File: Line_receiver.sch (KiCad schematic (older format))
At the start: 15 parts, among them U15 LM4562

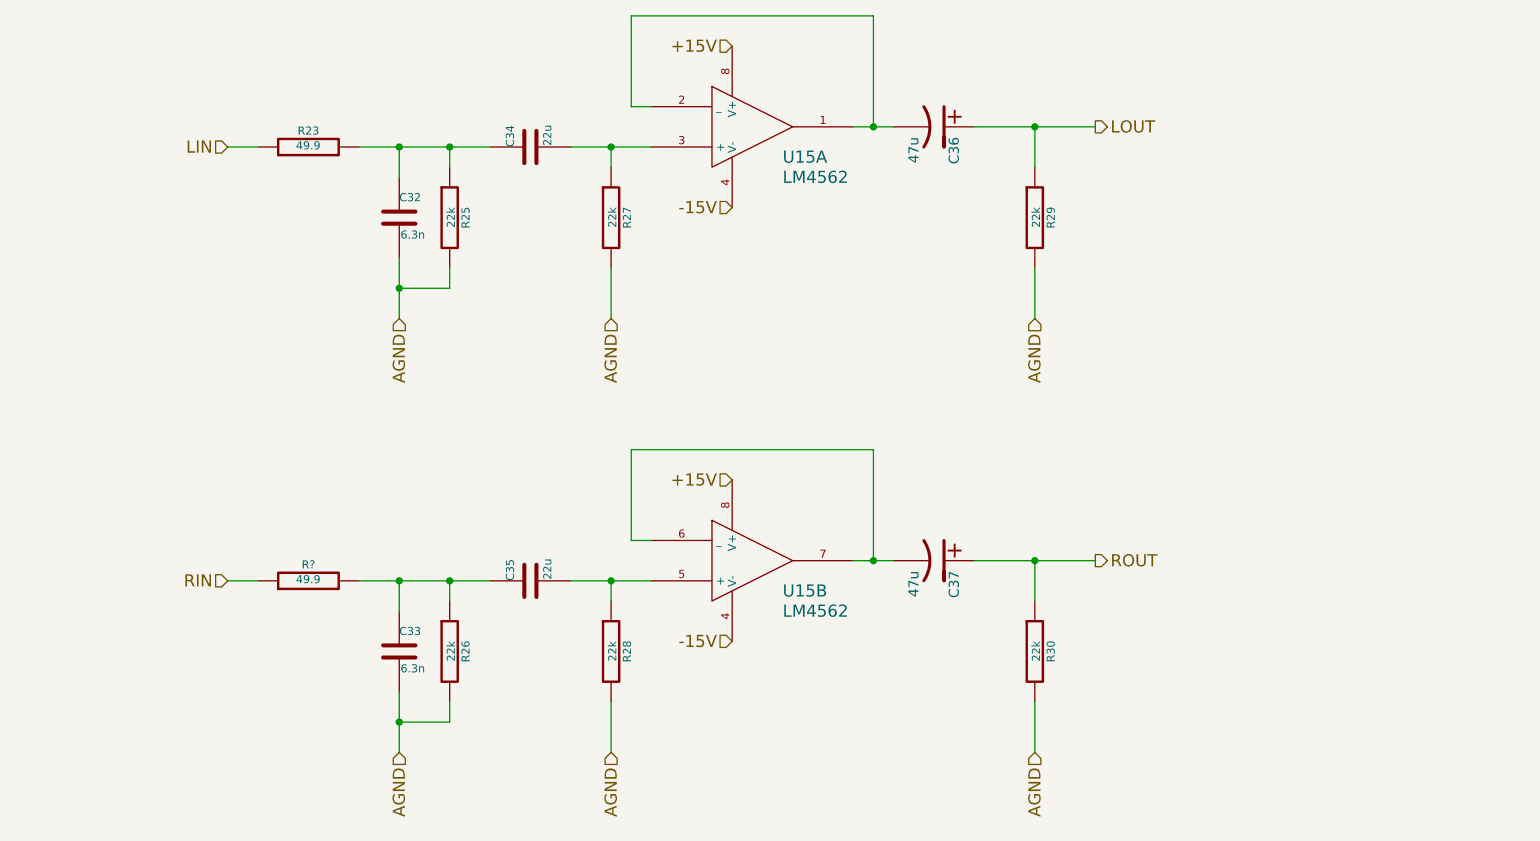
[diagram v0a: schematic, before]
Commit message: Further component specifications for the BOM.
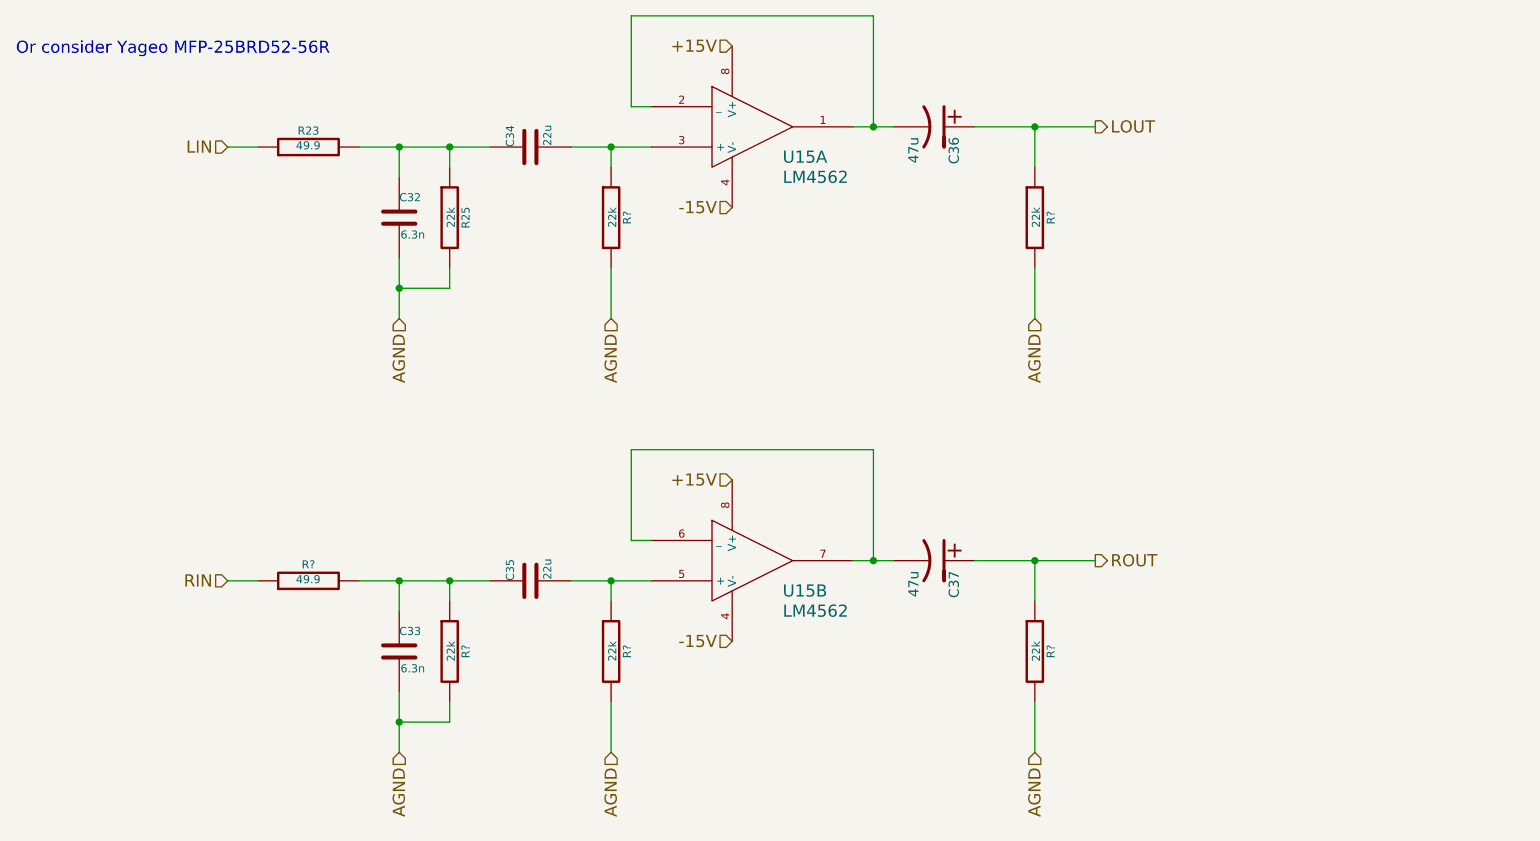
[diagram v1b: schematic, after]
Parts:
- removed R26, R27, R28, R29, R30: 22k, ~, symbol R
- added R? (x5): 22k, ~, symbol R
- R25: DigiKey (none) -> S22CACT-ND
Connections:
- net AGND: now also R?.2, R?.2, R?.2, R?.2, R?.2
- net LOUT: now also R?.1
- net ROUT: now also R?.1
- net at C34.2, U15.3 (+): now also R?.1
- net at C33.1, C35.1, R?.2: now also R?.1
- net at C35.2, U15.5 (+): now also R?.1
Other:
- note added: "Or consider Yageo MFP-25BRD52-56R"
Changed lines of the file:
@@
 LIBS:my-conn
 LIBS:ADC-cache
-EELAYER 24 0
+EELAYER 27 0
 EELAYER END
 $Descr A4 11693 8268
@@
 Sheet 4 6
 Title ""
-Date "21 may 2014"
+Date "23 may 2014"
 Rev ""
 Comp ""
@@
 F 2 "~" V 4030 3050 30  0000 C CNN
 F 3 "~" H 4100 3050 30  0000 C CNN
+F 4 "S22CACT-ND" V 4100 3050 60  0001 C CNN "DigiKey"
 	1    4100 3050
-	1    0    0    -1
-$EndComp
-$Comp
-L R R27
-U 1 1 536E0331
-P 4900 3050
-F 0 "R27" V 4980 3050 40  0000 C CNN
-F 1 "22k" V 4907 3051 40  0000 C CNN
-F 2 "~" V 4830 3050 30  0000 C CNN
-F 3 "~" H 4900 3050 30  0000 C CNN
-	1    4900 3050
 	1    0    0    -1
 $EndComp
@@
 $EndComp
 $Comp
-L R R26
-U 1 1 536E0AE6
-P 4100 5200
-F 0 "R26" V 4180 5200 40  0000 C CNN
-F 1 "22k" V 4107 5201 40  0000 C CNN
-F 2 "~" V 4030 5200 30  0000 C CNN
-F 3 "~" H 4100 5200 30  0000 C CNN
-	1    4100 5200
-	1    0    0    -1
-$EndComp
-$Comp
-L R R28
-U 1 1 536E0AEC
-P 4900 5200
-F 0 "R28" V 4980 5200 40  0000 C CNN
-F 1 "22k" V 4907 5201 40  0000 C CNN
-F 2 "~" V 4830 5200 30  0000 C CNN
-F 3 "~" H 4900 5200 30  0000 C CNN
-	1    4900 5200
-	1    0    0    -1
-$EndComp
-$Comp
 L LM4562 U15
 U 2 1 536E0AF2
@@
 Wire Wire Line
 	7000 4950 7000 4750
-$Comp
-L R R30
-U 1 1 536E0B02
-P 7000 5200
-F 0 "R30" V 7080 5200 40  0000 C CNN
-F 1 "22k" V 7007 5201 40  0000 C CNN
-F 2 "~" V 6930 5200 30  0000 C CNN
-F 3 "~" H 7000 5200 30  0000 C CNN
-	1    7000 5200
-	1    0    0    -1
-$EndComp
 Text HLabel 7000 3550 3    60   Input ~ 0
 AGND
 Wire Wire Line
 	7000 3300 7000 3550
-$Comp
-L R R29
-U 1 1 536E0334
-P 7000 3050
-F 0 "R29" V 7080 3050 40  0000 C CNN
-F 1 "22k" V 7007 3051 40  0000 C CNN
-F 2 "~" V 6930 3050 30  0000 C CNN
-F 3 "~" H 7000 3050 30  0000 C CNN
-	1    7000 3050
-	1    0    0    -1
-$EndComp
 Connection ~ 7000 2600
 Wire Wire Line
@@
 	0    -1   -1   0
 $EndComp
+$Comp
+L R R?
+U 1 1 537F34AE
+P 4900 3050
+F 0 "R?" V 4980 3050 40  0000 C CNN
+F 1 "22k" V 4907 3051 40  0000 C CNN
+F 2 "~" V 4830 3050 30  0000 C CNN
+F 3 "~" H 4900 3050 30  0000 C CNN
+F 4 "S22CACT-ND" V 4900 3050 60  0001 C CNN "DigiKey"
+	1    4900 3050
+	1    0    0    -1
+$EndComp
+$Comp
+L R R?
+U 1 1 537F34B5
+P 7000 3050
+F 0 "R?" V 7080 3050 40  0000 C CNN
+F 1 "22k" V 7007 3051 40  0000 C CNN
+F 2 "~" V 6930 3050 30  0000 C CNN
+F 3 "~" H 7000 3050 30  0000 C CNN
+F 4 "S22CACT-ND" V 7000 3050 60  0001 C CNN "DigiKey"
+	1    7000 3050
+	1    0    0    -1
+$EndComp
+$Comp
+L R R?
+U 1 1 537F34BC
+P 4100 5200
+F 0 "R?" V 4180 5200 40  0000 C CNN
+F 1 "22k" V 4107 5201 40  0000 C CNN
+F 2 "~" V 4030 5200 30  0000 C CNN
+F 3 "~" H 4100 5200 30  0000 C CNN
+F 4 "S22CACT-ND" V 4100 5200 60  0001 C CNN "DigiKey"
+	1    4100 5200
+	1    0    0    -1
+$EndComp
+$Comp
+L R R?
+U 1 1 537F34C3
+P 4900 5200
+F 0 "R?" V 4980 5200 40  0000 C CNN
+F 1 "22k" V 4907 5201 40  0000 C CNN
+F 2 "~" V 4830 5200 30  0000 C CNN
+F 3 "~" H 4900 5200 30  0000 C CNN
+F 4 "S22CACT-ND" V 4900 5200 60  0001 C CNN "DigiKey"
+	1    4900 5200
+	1    0    0    -1
+$EndComp
+$Comp
+L R R?
+U 1 1 537F34CA
+P 7000 5200
+F 0 "R?" V 7080 5200 40  0000 C CNN
+F 1 "22k" V 7007 5201 40  0000 C CNN
+F 2 "~" V 6930 5200 30  0000 C CNN
+F 3 "~" H 7000 5200 30  0000 C CNN
+F 4 "S22CACT-ND" V 7000 5200 60  0001 C CNN "DigiKey"
+	1    7000 5200
+	1    0    0    -1
+$EndComp
+Text Notes 1950 2250 0    60   ~ 0
+Or consider Yageo MFP-25BRD52-56R
 $EndSCHEMATC

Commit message: More components specified
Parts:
- removed R?: 49.9, ~, symbol R
- removed U15: LM4562, symbol LM4562
- added R24: 56, ~, symbol R
- added U15, U16: LME49740, ~, symbol LME49740
- C34: renamed from C32; value 6.3n -> 6.2n; DigiKey (none) -> P15430-ND
- C35: renamed from C33; value 6.3n -> 6.2n; DigiKey (none) -> P15430-ND
- C36: renamed from C34; DigiKey (none) -> P1188-ND
- C37: renamed from C35; DigiKey (none) -> P1188-ND
- C38: renamed from C36; DigiKey (none) -> P12923-ND
- C39: renamed from C37; DigiKey (none) -> P12923-ND
- R23: value 49.9 -> 56; DigiKey CMF49.9HFCT-ND -> 56ADCT-ND
- gave numbers to parts that had none: 5
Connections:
- net +15V: now also U15.4 (V+), U16.4 (V+)
- net -15V: now also U15.11 (V-), U16.11 (V-)
- net RIN: now also R24.1
- net at C36.2, R27.1: now also U15.3 (+)
- net at C38.2: now also U15.1, U15.2 (_)
- net at C35.1, C37.1, R26.1: now also R24.2
- net at C37.2, R28.1: now also U16.3 (+)
- net at C39.2: now also U16.1, U16.2 (_)
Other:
- note removed: "Or consider Yageo MFP-25BRD52-56R"
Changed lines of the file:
@@
 Sheet 4 6
 Title ""
-Date "23 may 2014"
+Date "25 may 2014"
 Rev ""
 Comp ""
@@
 P 3400 2700
 F 0 "R23" V 3480 2700 40  0000 C CNN
-F 1 "49.9" V 3407 2701 40  0000 C CNN
+F 1 "56" V 3407 2701 40  0000 C CNN
 F 2 "~" V 3330 2700 30  0000 C CNN
 F 3 "~" H 3400 2700 30  0000 C CNN
-F 4 "CMF49.9HFCT-ND" V 3400 2700 60  0001 C CNN "DigiKey"
+F 4 "56ADCT-ND" V 3400 2700 60  0001 C CNN "DigiKey"
 	1    3400 2700
 	0    -1   -1   0
 $EndComp
 $Comp
-L C C32
+L C C34
 U 1 1 536E032E
 P 3850 3050
-F 0 "C32" H 3850 3150 40  0000 L CNN
-F 1 "6.3n" H 3856 2965 40  0000 L CNN
+F 0 "C34" H 3850 3150 40  0000 L CNN
+F 1 "6.2n" H 3856 2965 40  0000 L CNN
 F 2 "~" H 3888 2900 30  0000 C CNN
 F 3 "~" H 3850 3050 60  0000 C CNN
+F 4 "P15430-ND" H 3850 3050 60  0001 C CNN "DigiKey"
 	1    3850 3050
 	1    0    0    -1
 $EndComp
 $Comp
-L C C34
+L C C36
 U 1 1 536E032F
 P 4500 2700
-F 0 "C34" H 4500 2800 40  0000 L CNN
+F 0 "C36" H 4500 2800 40  0000 L CNN
 F 1 "22u" H 4506 2615 40  0000 L CNN
 F 2 "~" H 4538 2550 30  0000 C CNN
 F 3 "~" H 4500 2700 60  0000 C CNN
+F 4 "P1188-ND" H 4500 2700 60  0001 C CNN "DigiKey"
 	1    4500 2700
 	0    -1   -1   0
@@
 	1    0    0    -1
 $EndComp
-$Comp
-L LM4562 U15
-U 1 1 536E0332
-P 5500 2600
-F 0 "U15" H 5750 2450 60  0000 L CNN
-F 1 "LM4562" H 5750 2350 60  0000 L CNN
-F 2 "" H 5600 2600 60  0000 C CNN
-F 3 "" H 5600 2600 60  0000 C CNN
-	1    5500 2600
-	1    0    0    -1
-$EndComp
 Text HLabel 5500 2200 0    60   Input ~ 0
 +15V
@@
 -15V
 $Comp
-L CP1 C36
+L CP1 C38
 U 1 1 536E0333
 P 6500 2600
-F 0 "C36" H 6550 2700 50  0000 L CNN
+F 0 "C38" H 6550 2700 50  0000 L CNN
 F 1 "47u" H 6550 2500 50  0000 L CNN
 F 2 "~" H 6500 2600 60  0000 C CNN
 F 3 "~" H 6500 2600 60  0000 C CNN
+F 4 "P12923-ND" H 6500 2600 60  0001 C CNN "DigiKey"
 	1    6500 2600
 	0    1    1    0
@@
 	7300 2600 6700 2600
 $Comp
-L C C33
+L C C35
 U 1 1 536E0ADA
 P 3850 5200
-F 0 "C33" H 3850 5300 40  0000 L CNN
-F 1 "6.3n" H 3856 5115 40  0000 L CNN
+F 0 "C35" H 3850 5300 40  0000 L CNN
+F 1 "6.2n" H 3856 5115 40  0000 L CNN
 F 2 "~" H 3888 5050 30  0000 C CNN
 F 3 "~" H 3850 5200 60  0000 C CNN
+F 4 "P15430-ND" H 3850 5200 60  0001 C CNN "DigiKey"
 	1    3850 5200
 	1    0    0    -1
 $EndComp
 $Comp
-L C C35
+L C C37
 U 1 1 536E0AE0
 P 4500 4850
-F 0 "C35" H 4500 4950 40  0000 L CNN
+F 0 "C37" H 4500 4950 40  0000 L CNN
 F 1 "22u" H 4506 4765 40  0000 L CNN
 F 2 "~" H 4538 4700 30  0000 C CNN
 F 3 "~" H 4500 4850 60  0000 C CNN
+F 4 "P1188-ND" H 4500 4850 60  0001 C CNN "DigiKey"
 	1    4500 4850
 	0    -1   -1   0
-$EndComp
-$Comp
-L LM4562 U15
-U 2 1 536E0AF2
-P 5500 4750
-F 0 "U15" H 5750 4600 60  0000 L CNN
-F 1 "LM4562" H 5750 4500 60  0000 L CNN
-F 2 "" H 5600 4750 60  0000 C CNN
-F 3 "" H 5600 4750 60  0000 C CNN
-	2    5500 4750
-	1    0    0    -1
 $EndComp
 Text HLabel 5500 4350 0    60   Input ~ 0
@@
 -15V
 $Comp
-L CP1 C37
+L CP1 C39
 U 1 1 536E0AFC
 P 6500 4750
-F 0 "C37" H 6550 4850 50  0000 L CNN
+F 0 "C39" H 6550 4850 50  0000 L CNN
 F 1 "47u" H 6550 4650 50  0000 L CNN
 F 2 "~" H 6500 4750 60  0000 C CNN
 F 3 "~" H 6500 4750 60  0000 C CNN
+F 4 "P12923-ND" H 6500 4750 60  0001 C CNN "DigiKey"
 	1    6500 4750
 	0    1    1    0
@@
 	7000 2800 7000 2600
 $Comp
-L R R?
-U 1 1 537DAD27
-P 3400 4850
-F 0 "R?" V 3480 4850 40  0000 C CNN
-F 1 "49.9" V 3407 4851 40  0000 C CNN
-F 2 "~" V 3330 4850 30  0000 C CNN
-F 3 "~" H 3400 4850 30  0000 C CNN
-F 4 "CMF49.9HFCT-ND" V 3400 4850 60  0001 C CNN "DigiKey"
-	1    3400 4850
-	0    -1   -1   0
-$EndComp
-$Comp
-L R R?
+L R R27
 U 1 1 537F34AE
 P 4900 3050
-F 0 "R?" V 4980 3050 40  0000 C CNN
+F 0 "R27" V 4980 3050 40  0000 C CNN
 F 1 "22k" V 4907 3051 40  0000 C CNN
 F 2 "~" V 4830 3050 30  0000 C CNN
@@
 $EndComp
 $Comp
-L R R?
+L R R29
 U 1 1 537F34B5
 P 7000 3050
-F 0 "R?" V 7080 3050 40  0000 C CNN
+F 0 "R29" V 7080 3050 40  0000 C CNN
 F 1 "22k" V 7007 3051 40  0000 C CNN
 F 2 "~" V 6930 3050 30  0000 C CNN
@@
 $EndComp
 $Comp
-L R R?
+L R R26
 U 1 1 537F34BC
 P 4100 5200
-F 0 "R?" V 4180 5200 40  0000 C CNN
+F 0 "R26" V 4180 5200 40  0000 C CNN
 F 1 "22k" V 4107 5201 40  0000 C CNN
 F 2 "~" V 4030 5200 30  0000 C CNN
@@
 $EndComp
 $Comp
-L R R?
+L R R28
 U 1 1 537F34C3
 P 4900 5200
-F 0 "R?" V 4980 5200 40  0000 C CNN
+F 0 "R28" V 4980 5200 40  0000 C CNN
 F 1 "22k" V 4907 5201 40  0000 C CNN
 F 2 "~" V 4830 5200 30  0000 C CNN
@@
 $EndComp
 $Comp
-L R R?
+L R R30
 U 1 1 537F34CA
 P 7000 5200
-F 0 "R?" V 7080 5200 40  0000 C CNN
+F 0 "R30" V 7080 5200 40  0000 C CNN
 F 1 "22k" V 7007 5201 40  0000 C CNN
 F 2 "~" V 6930 5200 30  0000 C CNN
@@
 	1    0    0    -1
 $EndComp
-Text Notes 1950 2250 0    60   ~ 0
-Or consider Yageo MFP-25BRD52-56R
+$Comp
+L R R24
+U 1 1 53802423
+P 3400 4850
+F 0 "R24" V 3480 4850 40  0000 C CNN
+F 1 "56" V 3407 4851 40  0000 C CNN
+F 2 "~" V 3330 4850 30  0000 C CNN
+F 3 "~" H 3400 4850 30  0000 C CNN
+F 4 "56ADCT-ND" V 3400 4850 60  0001 C CNN "DigiKey"
+	1    3400 4850
+	0    -1   -1   0
+$EndComp
+$Comp
+L LME49740 U15
+U 1 1 53803254
+P 5500 2600
+F 0 "U15" H 5750 2450 60  0000 L CNN
+F 1 "LME49740" H 5750 2350 60  0000 L CNN
+F 2 "~" H 5600 2600 60  0000 C CNN
+F 3 "~" H 5600 2600 60  0000 C CNN
+F 4 "LME49740NA/NOPB-ND" H 5500 2600 60  0001 C CNN "DigiKey"
+	1    5500 2600
+	1    0    0    -1
+$EndComp
+$Comp
+L LME49740 U16
+U 1 1 53803263
+P 5500 4750
+F 0 "U16" H 5750 4600 60  0000 L CNN
+F 1 "LME49740" H 5750 4500 60  0000 L CNN
+F 2 "~" H 5600 4750 60  0000 C CNN
+F 3 "~" H 5600 4750 60  0000 C CNN
+F 4 "LME49740NA/NOPB-ND" H 5500 4750 60  0001 C CNN "DigiKey"
+	1    5500 4750
+	1    0    0    -1
+$EndComp
 $EndSCHEMATC

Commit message: More footprint specification and connector additions; almost done.
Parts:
- C34, C35: footprint ~ -> Capacitors_ThroughHole:Capacitor18x7RM15
- C36, C37: footprint ~ -> Capacitors_ThroughHole:Capacitor5x11RM2.5
- C38, C39: footprint ~ -> Capacitors_Elko_ThroughHole:Elko_vert_DM5_RM2
- R23, R24, R25, R26, R27, R28, R29, R30: footprint ~ -> Resistors_ThroughHole:Resistor_Horizontal_RM10mm
- U15, U16: footprint ~ -> Sockets_DIP:DIP-14__300_ELL
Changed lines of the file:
@@
 F 0 "R23" V 3480 2700 40  0000 C CNN
 F 1 "56" V 3407 2701 40  0000 C CNN
-F 2 "~" V 3330 2700 30  0000 C CNN
+F 2 "Resistors_ThroughHole:Resistor_Horizontal_RM10mm" V 3330 2700 30  0001 C CNN
 F 3 "~" H 3400 2700 30  0000 C CNN
 F 4 "56ADCT-ND" V 3400 2700 60  0001 C CNN "DigiKey"
@@
 F 0 "C34" H 3850 3150 40  0000 L CNN
 F 1 "6.2n" H 3856 2965 40  0000 L CNN
-F 2 "~" H 3888 2900 30  0000 C CNN
+F 2 "Capacitors_ThroughHole:Capacitor18x7RM15" H 3888 2900 30  0001 C CNN
 F 3 "~" H 3850 3050 60  0000 C CNN
 F 4 "P15430-ND" H 3850 3050 60  0001 C CNN "DigiKey"
@@
 F 0 "C36" H 4500 2800 40  0000 L CNN
 F 1 "22u" H 4506 2615 40  0000 L CNN
-F 2 "~" H 4538 2550 30  0000 C CNN
+F 2 "Capacitors_ThroughHole:Capacitor5x11RM2.5" H 4538 2550 30  0001 C CNN
 F 3 "~" H 4500 2700 60  0000 C CNN
 F 4 "P1188-ND" H 4500 2700 60  0001 C CNN "DigiKey"
@@
 F 0 "R25" V 4180 3050 40  0000 C CNN
 F 1 "22k" V 4107 3051 40  0000 C CNN
-F 2 "~" V 4030 3050 30  0000 C CNN
+F 2 "Resistors_ThroughHole:Resistor_Horizontal_RM10mm" V 4030 3050 30  0001 C CNN
 F 3 "~" H 4100 3050 30  0000 C CNN
 F 4 "S22CACT-ND" V 4100 3050 60  0001 C CNN "DigiKey"
@@
 F 0 "C38" H 6550 2700 50  0000 L CNN
 F 1 "47u" H 6550 2500 50  0000 L CNN
-F 2 "~" H 6500 2600 60  0000 C CNN
+F 2 "Capacitors_Elko_ThroughHole:Elko_vert_DM5_RM2" H 6500 2600 60  0001 C CNN
 F 3 "~" H 6500 2600 60  0000 C CNN
 F 4 "P12923-ND" H 6500 2600 60  0001 C CNN "DigiKey"
@@
 F 0 "C35" H 3850 5300 40  0000 L CNN
 F 1 "6.2n" H 3856 5115 40  0000 L CNN
-F 2 "~" H 3888 5050 30  0000 C CNN
+F 2 "Capacitors_ThroughHole:Capacitor18x7RM15" H 3888 5050 30  0001 C CNN
 F 3 "~" H 3850 5200 60  0000 C CNN
 F 4 "P15430-ND" H 3850 5200 60  0001 C CNN "DigiKey"
@@
 F 0 "C37" H 4500 4950 40  0000 L CNN
 F 1 "22u" H 4506 4765 40  0000 L CNN
-F 2 "~" H 4538 4700 30  0000 C CNN
+F 2 "Capacitors_ThroughHole:Capacitor5x11RM2.5" H 4538 4700 30  0001 C CNN
 F 3 "~" H 4500 4850 60  0000 C CNN
 F 4 "P1188-ND" H 4500 4850 60  0001 C CNN "DigiKey"
@@
 F 0 "C39" H 6550 4850 50  0000 L CNN
 F 1 "47u" H 6550 4650 50  0000 L CNN
-F 2 "~" H 6500 4750 60  0000 C CNN
+F 2 "Capacitors_Elko_ThroughHole:Elko_vert_DM5_RM2" H 6500 4750 60  0001 C CNN
 F 3 "~" H 6500 4750 60  0000 C CNN
 F 4 "P12923-ND" H 6500 4750 60  0001 C CNN "DigiKey"
@@
 F 0 "R27" V 4980 3050 40  0000 C CNN
 F 1 "22k" V 4907 3051 40  0000 C CNN
-F 2 "~" V 4830 3050 30  0000 C CNN
+F 2 "Resistors_ThroughHole:Resistor_Horizontal_RM10mm" V 4830 3050 30  0001 C CNN
 F 3 "~" H 4900 3050 30  0000 C CNN
 F 4 "S22CACT-ND" V 4900 3050 60  0001 C CNN "DigiKey"
@@
 F 0 "R29" V 7080 3050 40  0000 C CNN
 F 1 "22k" V 7007 3051 40  0000 C CNN
-F 2 "~" V 6930 3050 30  0000 C CNN
+F 2 "Resistors_ThroughHole:Resistor_Horizontal_RM10mm" V 6930 3050 30  0001 C CNN
 F 3 "~" H 7000 3050 30  0000 C CNN
 F 4 "S22CACT-ND" V 7000 3050 60  0001 C CNN "DigiKey"
@@
 F 0 "R26" V 4180 5200 40  0000 C CNN
 F 1 "22k" V 4107 5201 40  0000 C CNN
-F 2 "~" V 4030 5200 30  0000 C CNN
+F 2 "Resistors_ThroughHole:Resistor_Horizontal_RM10mm" V 4030 5200 30  0001 C CNN
 F 3 "~" H 4100 5200 30  0000 C CNN
 F 4 "S22CACT-ND" V 4100 5200 60  0001 C CNN "DigiKey"
@@
 F 0 "R28" V 4980 5200 40  0000 C CNN
 F 1 "22k" V 4907 5201 40  0000 C CNN
-F 2 "~" V 4830 5200 30  0000 C CNN
+F 2 "Resistors_ThroughHole:Resistor_Horizontal_RM10mm" V 4830 5200 30  0001 C CNN
 F 3 "~" H 4900 5200 30  0000 C CNN
 F 4 "S22CACT-ND" V 4900 5200 60  0001 C CNN "DigiKey"
@@
 F 0 "R30" V 7080 5200 40  0000 C CNN
 F 1 "22k" V 7007 5201 40  0000 C CNN
-F 2 "~" V 6930 5200 30  0000 C CNN
+F 2 "Resistors_ThroughHole:Resistor_Horizontal_RM10mm" V 6930 5200 30  0001 C CNN
 F 3 "~" H 7000 5200 30  0000 C CNN
 F 4 "S22CACT-ND" V 7000 5200 60  0001 C CNN "DigiKey"
@@
 F 0 "R24" V 3480 4850 40  0000 C CNN
 F 1 "56" V 3407 4851 40  0000 C CNN
-F 2 "~" V 3330 4850 30  0000 C CNN
+F 2 "Resistors_ThroughHole:Resistor_Horizontal_RM10mm" V 3330 4850 30  0001 C CNN
 F 3 "~" H 3400 4850 30  0000 C CNN
 F 4 "56ADCT-ND" V 3400 4850 60  0001 C CNN "DigiKey"
@@
 F 0 "U15" H 5750 2450 60  0000 L CNN
 F 1 "LME49740" H 5750 2350 60  0000 L CNN
-F 2 "~" H 5600 2600 60  0000 C CNN
+F 2 "Sockets_DIP:DIP-14__300_ELL" H 5600 2600 60  0001 C CNN
 F 3 "~" H 5600 2600 60  0000 C CNN
 F 4 "LME49740NA/NOPB-ND" H 5500 2600 60  0001 C CNN "DigiKey"
@@
 F 0 "U16" H 5750 4600 60  0000 L CNN
 F 1 "LME49740" H 5750 4500 60  0000 L CNN
-F 2 "~" H 5600 4750 60  0000 C CNN
+F 2 "Sockets_DIP:DIP-14__300_ELL" H 5600 4750 60  0001 C CNN
 F 3 "~" H 5600 4750 60  0000 C CNN
 F 4 "LME49740NA/NOPB-ND" H 5500 4750 60  0001 C CNN "DigiKey"
